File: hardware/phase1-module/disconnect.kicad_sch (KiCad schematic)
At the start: 16 parts, among them Q3 60V NFET, Q4 60V NFET, Q7 2N7002, Q9 2N7002, U6 LTC7004, U7 TLV7011

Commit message: Apply China-sourcing engineering changes across all boards + mechanical frame
All datasheet-verified before application (details hardware/SOURCING.md sF):
- TMUX1101 -> TS5A3166DBVR (LCSC availability; ts5a3166.pdf: pin POSITIONS
  identical - 1=NO 2=COM 3=GND 4=IN 5=V+; VIH 2.4V ok from 3.3V GPIO)
- TLV7011 DBVR -> DCKR: tlv7022.pdf shows DBV/DCK share one pinout, so
  footprint-only (SOT-353_SC-70-5); SOT-23-5 stock in China is nearly gone
- crystal load caps 10p -> 18p, both phases (CL=12pF China crystals; the
  HANDOVER-blessed alternative to hunting CL=8pF parts)
- Phase-1 inductor -> MWSA1707S-100MT (JLCPCB-verified 16.5A Isat/10.5A
  Irms vs 12A/8A required); value strings now dual-source Sunlord/Coilcraft
- module slot power + P2 output -> XT60PW-M (2-pin), backplane slots ->
  XT60PW-F; bus shunt -> 2x BVS-M-R0005 parallel (the exact-net checker
  caught RS1/RS2 placed one pin-span apart merging VBUS_IN into VBUS)
- 470u bulk -> THT radial D10; output MLCCs 22u -> 10u/50V X7S; buzzer ->
  MLT-8530 (fp placeholder)
All four checker chains green: 137/173/30/80 components.

hardware/MECHANICAL.md (frozen): 30mm slot pitch, P2 130x90 4-layer,
backplane ~330x100 2-layer 2oz, manager 100x80; cost-first stackup (1oz
outer + solder-reinforced bus, 2oz only if the thermal soak demands it);
inductor footprint = SUPERSET pattern accepting Sunlord 1707 AND Coilcraft
XAL1510 so the A/B pair is a pure part swap.

HANDOVER: sub-0.5V mV-accurate output DEFERRED to a future dedicated
linear post-regulator module (user decision 2026-07-18); buck floors
documented (P2 0.7V @30V bus, P1 0.5V).

Co-Authored-By: Claude Fable 5 <noreply@anthropic.com>
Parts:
- U7: value TLV7011 -> TLV7011DCK; footprint Package_TO_SOT_SMD:SOT-23-5 -> Package_TO_SOT_SMD:SOT-353_SC-70-5
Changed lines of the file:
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@@
     (in_bom yes) (on_board yes) (dnp no)
     (property "Reference" "U7" (at 165.1 123.19 0) (effects (font (size 1.27 1.27))))
-    (property "Value" "TLV7011" (at 165.1 135.89000000000001 0) (effects (font (size 1.27 1.27))))
-    (property "Footprint" "Package_TO_SOT_SMD:SOT-23-5" (at 165.1 127.0 0) (effects (font (size 1.27 1.27)) hide))
+    (property "Value" "TLV7011DCK" (at 165.1 135.89000000000001 0) (effects (font (size 1.27 1.27))))
+    (property "Footprint" "Package_TO_SOT_SMD:SOT-353_SC-70-5" (at 165.1 127.0 0) (effects (font (size 1.27 1.27)) hide))
     (property "Datasheet" "~" (at 165.1 127.0 0) (effects (font (size 1.27 1.27)) hide))
     (pin "1")

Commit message: Add LCSC part numbers to all four boards' schematics and generate BOMs
common/bom.py writes hidden LCSC/MPN/Manufacturer properties into the
placed symbols (additive only, both one-line and KiCad multi-line
property styles) and emits <board>/bom/<board>-bom.csv plus a
JLCPCB-format CSV. Part table in common/lcsc_parts.py, transcribed
from SOURCING.md with explicit references per board; CHECK notes flag
footprint/variant mismatches. --check fails on stale output.

Co-Authored-By: Claude Opus 5.5 (1M context) <noreply@anthropic.com>
Claude-Session: https://claude.ai/code/session_01MKtKgebN9BpUrgqHq9t7pT
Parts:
- U6: LCSC (none) -> C690105; MPN (none) -> LTC7004EMSE#PBF; Manufacturer (none) -> ADI
- U7: LCSC (none) -> C193688; MPN (none) -> TLV7011DCKR; Manufacturer (none) -> TI
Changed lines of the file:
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@@
     (property "Footprint" "Package_SO:MSOP-10-1EP_3x3mm_P0.5mm_EP1.68x1.88mm" (at 76.2 127.0 0) (effects (font (size 1.27 1.27)) hide))
     (property "Datasheet" "~" (at 76.2 127.0 0) (effects (font (size 1.27 1.27)) hide))
+    (property "LCSC" "C690105" (at 76.2 127.0 0) (effects (font (size 1.27 1.27)) hide))
+    (property "MPN" "LTC7004EMSE#PBF" (at 76.2 127.0 0) (effects (font (size 1.27 1.27)) hide))
+    (property "Manufacturer" "ADI" (at 76.2 127.0 0) (effects (font (size 1.27 1.27)) hide))
     (pin "1")
     (pin "10")
@@
     (property "Footprint" "Package_TO_SOT_SMD:SOT-353_SC-70-5" (at 165.1 127.0 0) (effects (font (size 1.27 1.27)) hide))
     (property "Datasheet" "~" (at 165.1 127.0 0) (effects (font (size 1.27 1.27)) hide))
+    (property "LCSC" "C193688" (at 165.1 127.0 0) (effects (font (size 1.27 1.27)) hide))
+    (property "MPN" "TLV7011DCKR" (at 165.1 127.0 0) (effects (font (size 1.27 1.27)) hide))
+    (property "Manufacturer" "TI" (at 165.1 127.0 0) (effects (font (size 1.27 1.27)) hide))
     (pin "1")
     (pin "2")

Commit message: Phase-1 BOM: Q3/Q4 part, hand-solder notes
Q3/Q4 (output disconnect, 60 V NFET on the SON5x6 GDS land) get the
same part as Q1/Q2: CSD18563Q5A, LCSC C77239, already verified in
SOURCING.md for this footprint. The through-hole parts (J1-J6, F1) are
marked hand-solder in the BOM notes. bom.py --check passes.

Co-Authored-By: Claude Opus 5.5 (1M context) <noreply@anthropic.com>
Claude-Session: https://claude.ai/code/session_017ZrT5TjsLMQoxTZy1jabew
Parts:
- Q3, Q4: LCSC (none) -> C77239; MPN (none) -> CSD18563Q5A; Manufacturer (none) -> TI
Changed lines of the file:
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@@
     (property "Footprint" "labbench:PowerFET_SON5x6_GDS" (at 96.52 63.5 0) (effects (font (size 1.27 1.27)) hide))
     (property "Datasheet" "~" (at 96.52 63.5 0) (effects (font (size 1.27 1.27)) hide))
+    (property "LCSC" "C77239" (at 96.52 63.5 0) (effects (font (size 1.27 1.27)) hide))
+    (property "MPN" "CSD18563Q5A" (at 96.52 63.5 0) (effects (font (size 1.27 1.27)) hide))
+    (property "Manufacturer" "TI" (at 96.52 63.5 0) (effects (font (size 1.27 1.27)) hide))
     (pin "1")
     (pin "2")
@@
     (property "Footprint" "labbench:PowerFET_SON5x6_GDS" (at 134.62 63.5 0) (effects (font (size 1.27 1.27)) hide))
     (property "Datasheet" "~" (at 134.62 63.5 0) (effects (font (size 1.27 1.27)) hide))
+    (property "LCSC" "C77239" (at 134.62 63.5 0) (effects (font (size 1.27 1.27)) hide))
+    (property "MPN" "CSD18563Q5A" (at 134.62 63.5 0) (effects (font (size 1.27 1.27)) hide))
+    (property "Manufacturer" "TI" (at 134.62 63.5 0) (effects (font (size 1.27 1.27)) hide))
     (pin "1")
     (pin "2")

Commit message: Phase-1 BOM: LCSC numbers for every assembled part
Fill the 109 missing Phase-1 placements from the JLCPCB catalogue
(checked 2026-09-27, Basic parts where one fits), so 127 of 136
placements carry an LCSC number. J1-J6 and F1 stay hand-solder;
C17 and R17 are DNP.

Out-of-stock swaps: Q1-Q4 CSD18563Q5A -> NTMFS5C670NLT1G (SO-8FL,
same pinout), P1 U5 INA228AIDGSR -> INA228AQDGSRQ1. Y1 moves to the
CL = 12 pF version of the same crystal (C400090 was the 10 pF one).

Co-Authored-By: Claude Opus 5.5 (1M context) <noreply@anthropic.com>
Claude-Session: https://claude.ai/code/session_013uVohQZFdivAh43gw4mZtf
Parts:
- C41, C43: LCSC (none) -> C14663; MPN (none) -> CC0603KRX7R9BB104; Manufacturer (none) -> YAGEO
- C42: LCSC (none) -> C15849; MPN (none) -> CL10A105KB8NNNC; Manufacturer (none) -> Samsung Electro-Mechanics
- C44: LCSC (none) -> C1588; MPN (none) -> CL10B102KB8NNNC; Manufacturer (none) -> Samsung Electro-Mechanics
- Q3, Q4: LCSC C77239 -> C179626; MPN CSD18563Q5A -> NTMFS5C670NLT1G; Manufacturer TI -> onsemi
- Q7, Q9: LCSC (none) -> C8545; MPN (none) -> 2N7002; Manufacturer (none) -> Jiangsu Changjing Electronics Technology Co., Ltd.
- R43, R47: LCSC (none) -> C25804; MPN (none) -> 0603WAF1002T5E; Manufacturer (none) -> UNI-ROYAL
- R44: LCSC (none) -> C25819; MPN (none) -> 0603WAF4702T5E; Manufacturer (none) -> UNI-ROYAL
- R45: LCSC (none) -> C22883; MPN (none) -> 0603WAF1583T5E; Manufacturer (none) -> UNI-ROYAL
- R46: LCSC (none) -> C4184; MPN (none) -> 0603WAF2002T5E; Manufacturer (none) -> UNI-ROYAL
- R48: LCSC (none) -> C25967; MPN (none) -> 0603WAF3162T5E; Manufacturer (none) -> UNI-ROYAL
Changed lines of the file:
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@@
     (property "Footprint" "labbench:PowerFET_SON5x6_GDS" (at 96.52 63.5 0) (effects (font (size 1.27 1.27)) hide))
     (property "Datasheet" "~" (at 96.52 63.5 0) (effects (font (size 1.27 1.27)) hide))
-    (property "LCSC" "C77239" (at 96.52 63.5 0) (effects (font (size 1.27 1.27)) hide))
-    (property "MPN" "CSD18563Q5A" (at 96.52 63.5 0) (effects (font (size 1.27 1.27)) hide))
-    (property "Manufacturer" "TI" (at 96.52 63.5 0) (effects (font (size 1.27 1.27)) hide))
+    (property "LCSC" "C179626" (at 96.52 63.5 0) (effects (font (size 1.27 1.27)) hide))
+    (property "MPN" "NTMFS5C670NLT1G" (at 96.52 63.5 0) (effects (font (size 1.27 1.27)) hide))
+    (property "Manufacturer" "onsemi" (at 96.52 63.5 0) (effects (font (size 1.27 1.27)) hide))
     (pin "1")
     (pin "2")
@@
     (property "Footprint" "labbench:PowerFET_SON5x6_GDS" (at 134.62 63.5 0) (effects (font (size 1.27 1.27)) hide))
     (property "Datasheet" "~" (at 134.62 63.5 0) (effects (font (size 1.27 1.27)) hide))
-    (property "LCSC" "C77239" (at 134.62 63.5 0) (effects (font (size 1.27 1.27)) hide))
-    (property "MPN" "CSD18563Q5A" (at 134.62 63.5 0) (effects (font (size 1.27 1.27)) hide))
-    (property "Manufacturer" "TI" (at 134.62 63.5 0) (effects (font (size 1.27 1.27)) hide))
+    (property "LCSC" "C179626" (at 134.62 63.5 0) (effects (font (size 1.27 1.27)) hide))
+    (property "MPN" "NTMFS5C670NLT1G" (at 134.62 63.5 0) (effects (font (size 1.27 1.27)) hide))
+    (property "Manufacturer" "onsemi" (at 134.62 63.5 0) (effects (font (size 1.27 1.27)) hide))
     (pin "1")
     (pin "2")
@@
     (property "Footprint" "Capacitor_SMD:C_0603_1608Metric" (at 113.03 121.92 0) (effects (font (size 1.27 1.27)) hide))
     (property "Datasheet" "~" (at 113.03 121.92 0) (effects (font (size 1.27 1.27)) hide))
+    (property "LCSC" "C14663" (at 113.03 121.92 0) (effects (font (size 1.27 1.27)) hide))
+    (property "MPN" "CC0603KRX7R9BB104" (at 113.03 121.92 0) (effects (font (size 1.27 1.27)) hide))
+    (property "Manufacturer" "YAGEO" (at 113.03 121.92 0) (effects (font (size 1.27 1.27)) hide))
     (pin "1")
     (pin "2")
@@
     (property "Footprint" "Capacitor_SMD:C_0603_1608Metric" (at 55.88 132.08 0) (effects (font (size 1.27 1.27)) hide))
     (property "Datasheet" "~" (at 55.88 132.08 0) (effects (font (size 1.27 1.27)) hide))
+    (property "LCSC" "C15849" (at 55.88 132.08 0) (effects (font (size 1.27 1.27)) hide))
+    (property "MPN" "CL10A105KB8NNNC" (at 55.88 132.08 0) (effects (font (size 1.27 1.27)) hide))
+    (property "Manufacturer" "Samsung Electro-Mechanics" (at 55.88 132.08 0) (effects (font (size 1.27 1.27)) hide))
     (pin "1")
     (pin "2")
@@
     (property "Footprint" "Resistor_SMD:R_0603_1608Metric" (at 41.91 111.76 0) (effects (font (size 1.27 1.27)) hide))
     (property "Datasheet" "~" (at 41.91 111.76 0) (effects (font (size 1.27 1.27)) hide))
+    (property "LCSC" "C25804" (at 41.91 111.76 0) (effects (font (size 1.27 1.27)) hide))
+    (property "MPN" "0603WAF1002T5E" (at 41.91 111.76 0) (effects (font (size 1.27 1.27)) hide))
+    (property "Manufacturer" "UNI-ROYAL" (at 41.91 111.76 0) (effects (font (size 1.27 1.27)) hide))
     (pin "1")
     (pin "2")
@@
     (property "Footprint" "Resistor_SMD:R_0603_1608Metric" (at 55.88 111.76 0) (effects (font (size 1.27 1.27)) hide))
     (property "Datasheet" "~" (at 55.88 111.76 0) (effects (font (size 1.27 1.27)) hide))
+    (property "LCSC" "C25819" (at 55.88 111.76 0) (effects (font (size 1.27 1.27)) hide))
+    (property "MPN" "0603WAF4702T5E" (at 55.88 111.76 0) (effects (font (size 1.27 1.27)) hide))
+    (property "Manufacturer" "UNI-ROYAL" (at 55.88 111.76 0) (effects (font (size 1.27 1.27)) hide))
     (pin "1")
     (pin "2")
@@
     (property "Footprint" "Package_TO_SOT_SMD:SOT-23" (at 33.02 137.16 0) (effects (font (size 1.27 1.27)) hide))
     (property "Datasheet" "~" (at 33.02 137.16 0) (effects (font (size 1.27 1.27)) hide))
+    (property "LCSC" "C8545" (at 33.02 137.16 0) (effects (font (size 1.27 1.27)) hide))
+    (property "MPN" "2N7002" (at 33.02 137.16 0) (effects (font (size 1.27 1.27)) hide))
+    (property "Manufacturer" "Jiangsu Changjing Electronics Technology Co., Ltd." (at 33.02 137.16 0) (effects (font (size 1.27 1.27)) hide))
     (pin "1")
     (pin "2")
@@
     (property "Footprint" "Resistor_SMD:R_0603_1608Metric" (at 146.05 96.52 0) (effects (font (size 1.27 1.27)) hide))
     (property "Datasheet" "~" (at 146.05 96.52 0) (effects (font (size 1.27 1.27)) hide))
+    (property "LCSC" "C22883" (at 146.05 96.52 0) (effects (font (size 1.27 1.27)) hide))
+    (property "MPN" "0603WAF1583T5E" (at 146.05 96.52 0) (effects (font (size 1.27 1.27)) hide))
+    (property "Manufacturer" "UNI-ROYAL" (at 146.05 96.52 0) (effects (font (size 1.27 1.27)) hide))
     (pin "1")
     (pin "2")
@@
     (property "Footprint" "Resistor_SMD:R_0603_1608Metric" (at 146.05 111.76 0) (effects (font (size 1.27 1.27)) hide))
     (property "Datasheet" "~" (at 146.05 111.76 0) (effects (font (size 1.27 1.27)) hide))
+    (property "LCSC" "C4184" (at 146.05 111.76 0) (effects (font (size 1.27 1.27)) hide))
+    (property "MPN" "0603WAF2002T5E" (at 146.05 111.76 0) (effects (font (size 1.27 1.27)) hide))
+    (property "Manufacturer" "UNI-ROYAL" (at 146.05 111.76 0) (effects (font (size 1.27 1.27)) hide))
     (pin "1")
     (pin "2")
@@
     (property "Footprint" "Capacitor_SMD:C_0603_1608Metric" (at 156.21 111.76 0) (effects (font (size 1.27 1.27)) hide))
     (property "Datasheet" "~" (at 156.21 111.76 0) (effects (font (size 1.27 1.27)) hide))
+    (property "LCSC" "C1588" (at 156.21 111.76 0) (effects (font (size 1.27 1.27)) hide))
+    (property "MPN" "CL10B102KB8NNNC" (at 156.21 111.76 0) (effects (font (size 1.27 1.27)) hide))
+    (property "Manufacturer" "Samsung Electro-Mechanics" (at 156.21 111.76 0) (effects (font (size 1.27 1.27)) hide))
     (pin "1")
     (pin "2")
@@
     (property "Footprint" "Resistor_SMD:R_0603_1608Metric" (at 190.5 96.52 0) (effects (font (size 1.27 1.27)) hide))
     (property "Datasheet" "~" (at 190.5 96.52 0) (effects (font (size 1.27 1.27)) hide))
+    (property "LCSC" "C25804" (at 190.5 96.52 0) (effects (font (size 1.27 1.27)) hide))
+    (property "MPN" "0603WAF1002T5E" (at 190.5 96.52 0) (effects (font (size 1.27 1.27)) hide))
+    (property "Manufacturer" "UNI-ROYAL" (at 190.5 96.52 0) (effects (font (size 1.27 1.27)) hide))
     (pin "1")
     (pin "2")
@@
     (property "Footprint" "Resistor_SMD:R_0603_1608Metric" (at 190.5 111.76 0) (effects (font (size 1.27 1.27)) hide))
     (property "Datasheet" "~" (at 190.5 111.76 0) (effects (font (size 1.27 1.27)) hide))
+    (property "LCSC" "C25967" (at 190.5 111.76 0) (effects (font (size 1.27 1.27)) hide))
+    (property "MPN" "0603WAF3162T5E" (at 190.5 111.76 0) (effects (font (size 1.27 1.27)) hide))
+    (property "Manufacturer" "UNI-ROYAL" (at 190.5 111.76 0) (effects (font (size 1.27 1.27)) hide))
     (pin "1")
     (pin "2")
@@
     (property "Footprint" "Capacitor_SMD:C_0603_1608Metric" (at 177.8 132.08 0) (effects (font (size 1.27 1.27)) hide))
     (property "Datasheet" "~" (at 177.8 132.08 0) (effects (font (size 1.27 1.27)) hide))
+    (property "LCSC" "C14663" (at 177.8 132.08 0) (effects (font (size 1.27 1.27)) hide))
+    (property "MPN" "CC0603KRX7R9BB104" (at 177.8 132.08 0) (effects (font (size 1.27 1.27)) hide))
+    (property "Manufacturer" "YAGEO" (at 177.8 132.08 0) (effects (font (size 1.27 1.27)) hide))
     (pin "1")
     (pin "2")
@@
     (property "Footprint" "Package_TO_SOT_SMD:SOT-23" (at 205.74 142.24 0) (effects (font (size 1.27 1.27)) hide))
     (property "Datasheet" "~" (at 205.74 142.24 0) (effects (font (size 1.27 1.27)) hide))
-    (pin "1")
-    (pin "2")
+    (property "LCSC" "C8545" (at 205.74 142.24 0) (effects (font (size 1.27 1.27)) hide))
+    (property "MPN" "2N7002" (at 205.74 142.24 0) (effects (font (size 1.27 1.27)) hide))
+    (property "Manufacturer" "Jiangsu Changjing Electronics Technology Co., Ltd." (at 205.74 142.24 0) (effects (font (size 1.27 1.27)) hide))
+    (pin "1")
+    (pin "2")

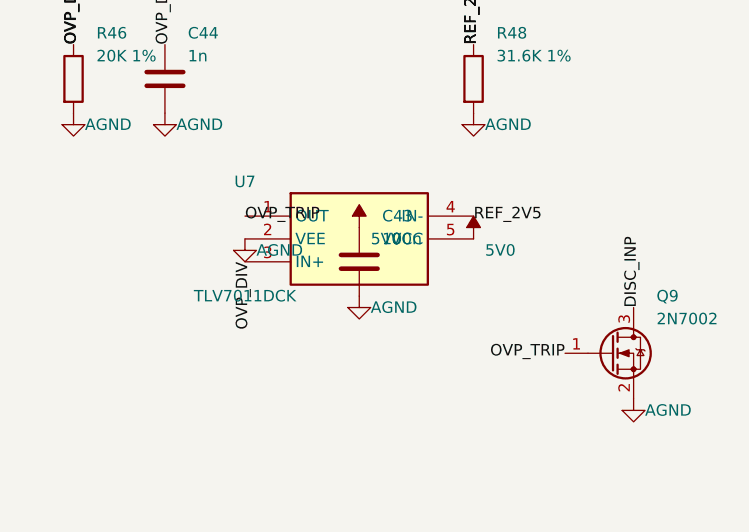
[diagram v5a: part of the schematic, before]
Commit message: Phase-1 board: route OVP_TRIP to MCU PB4 so the OVP trip can latch
The TLV7011 output only reached Q9 (disconnect), so an overvoltage
opened the output but left the LM5145 running and nothing latched.
OVP_TRIP now also goes to U10 pin 41 (PB4, a spare pin), where the
firmware 0.2 EXTI handler kills EN and latches OVP_HW.

Schematic: surgical edits (OVP_TRIP local labels -> global, PB4
no-connect -> OVP_TRIP label); gen_phase1.py / sheets_common.py
mirror it (ovp_to_mcu param, EXPECTED_NETS). check_netlist and
check_footprints pass.

Board: 21 signal nets in the U10-U7 region ripped and re-routed with
Freerouting 1.9 + finish_routes, fb_reroute rerun, three overlap stubs
trimmed. DRC: 0 unconnected, 0 errors, 10 silk warnings (was 11).
Fab zip regenerated; placement and BOM unchanged.

Co-Authored-By: Claude Opus 5.5 (1M context) <noreply@anthropic.com>
Claude-Session: https://claude.ai/code/session_01NmR2rbcK8CFj3PgzqsaRtW
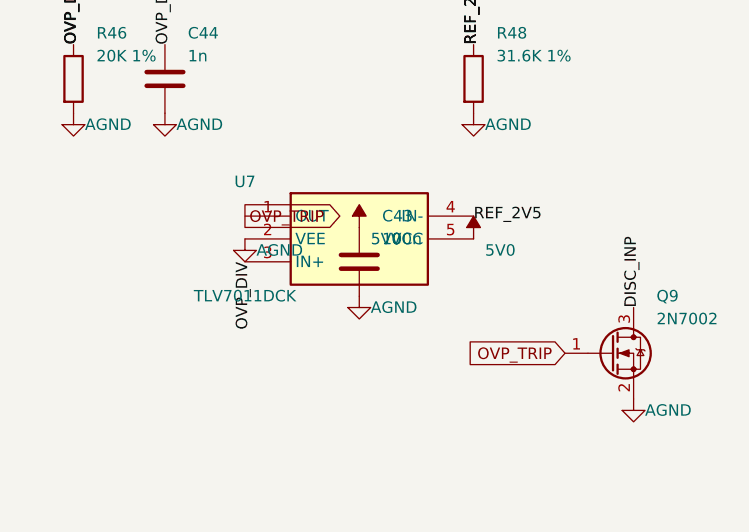
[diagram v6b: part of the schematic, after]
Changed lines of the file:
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@@
   (label "REF_2V5" (at 190.5 107.95 90) (effects (font (size 1.27 1.27))))
   (label "REF_2V5" (at 190.5 127.0 0) (effects (font (size 1.27 1.27))))
-  (label "OVP_TRIP" (at 165.1 127.0 0) (effects (font (size 1.27 1.27))))
-  (label "OVP_TRIP" (at 200.66 142.24 180) (effects (font (size 1.27 1.27))))
+  (global_label "OVP_TRIP" (shape output) (at 165.1 127.0 0) (fields_autoplaced) (effects (font (size 1.27 1.27))))
+  (global_label "OVP_TRIP" (shape input) (at 200.66 142.24 180) (fields_autoplaced) (effects (font (size 1.27 1.27))))
   (label "DISC_INP" (at 208.28 137.16 90) (effects (font (size 1.27 1.27))))
   (text "OUTPUT DISCONNECT: back-to-back NFETs (blocks battery back-feed when off),\nLTC7004 charge-pump gate driver. INP = OUT_REQ AND NOT(EN_KILL) AND NOT(OVP).\nOVP: VOUT_INT/8.9 vs 2.5V ref -> trips at 22.25V, independent of firmware." (at 33.02 33.02 0) (effects (font (size 1.27 1.27))))
